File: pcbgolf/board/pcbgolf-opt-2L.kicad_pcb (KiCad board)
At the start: 2 copper layers, 48.2 x 51 mm, 245 parts, among them J1 DCBARRELSMT, J2 MICRO_SD-0472192001, J3 USB-C-FEMALE, J4 CAN, J5 USB-C-FEMALEGCT, J6 USB-C-FEMALEGCT, J7 USB-C-FEMALEGCT, J8 USB-C-FEMALEGCT, Q1 SIS427-VI, Q2 NFET-DUAL-COMMON-SOURCE-QS5K2, Q3 NFET-DUAL-COMMON-SOURCE-QS5K2, Q4 NFET-DUAL-COMMON-SOURCE-QS5K2, Q5 NFET-DUAL-COMMON-SOURCE-QS5K2, Q6 NFET-DUAL-COMMON-SOURCE-QS5K2, Q7 NFET-DUAL-COMMON-SOURCE-QS5K2, Q8 NFET-DUAL-COMMON-SOURCE-QS5K2, Q9 NFET-DUAL-COMMON-SOURCE-QS5K2, SW1 SPST-2-4PIN, U1 AP62300T, U10 NCS20071XV, U11 NCS20071XV, U12 NCS20071XV, U13 TPS25942, U14 TPS25942, U15 TPS25942, U16 TPS25942, U2 AP62300T, U3 STM32H725ZGTx, U4 USB2517, U5 MCP2542FDT-E/MNY, U6 MCP2542FDT-E/MNY, U7 MCP2542FDT-E/MNY, U8 MCP2542FDT-E/MNY, U9 NCS20071XV, Y1 25MHz, Y2 24MHz

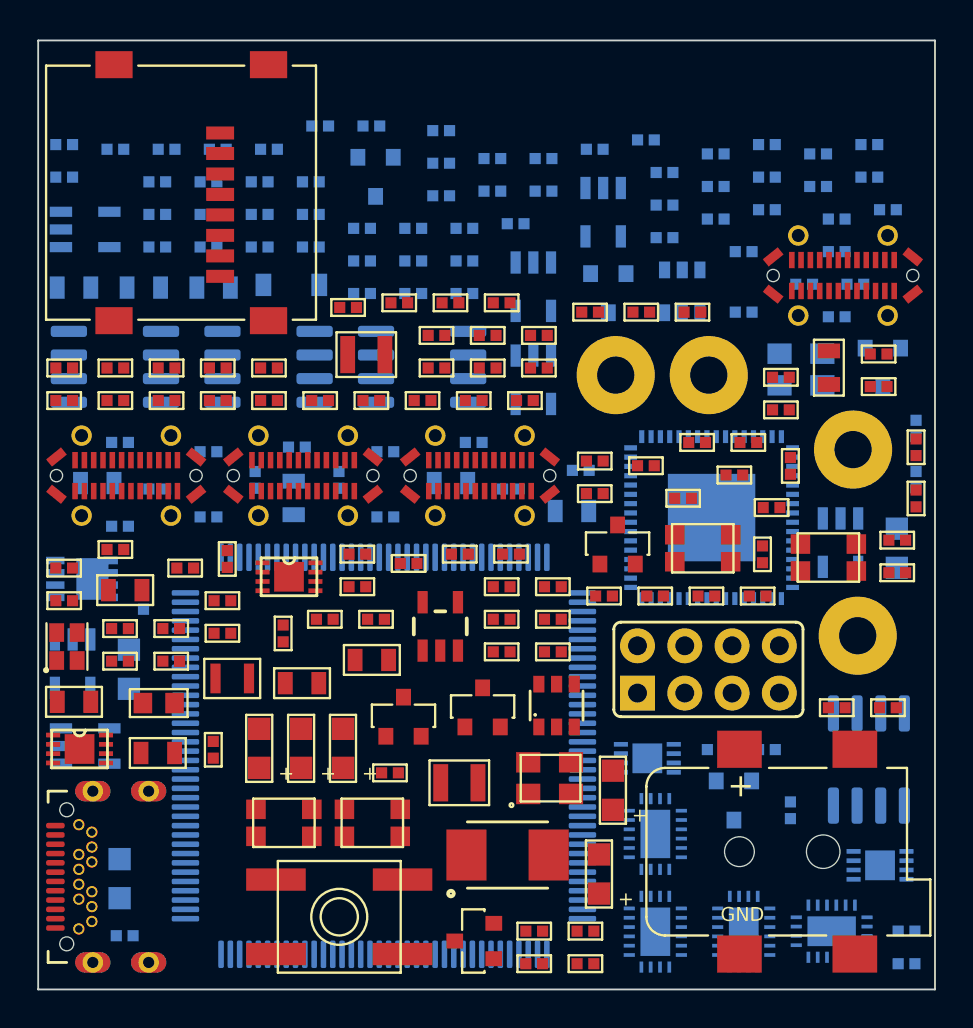
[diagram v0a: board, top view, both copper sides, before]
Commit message: Sync pcbgolf: measured part heights, 3D assembly bounding box, final board
Mirrors lblommesteyn/pcbgolf. The substantive change is that part heights are
now measured from the footprints' own STEP models rather than estimated: the
barrel jack is 11.00 mm, not the 9.00 mm assumed, so Z is 14.35 mm and every
previously reported volume was understated by about 5,300 mm^3.

Also adds bbox3d.py (the real PCBA bounding box, which is what the challenge
scores), step_assembly.py (a STEP built from that same geometry), and the
final LQFP-100 board with R11 not fitted, since the LQFP-100 package has no
PDR_ON pin for it to strap.

Co-Authored-By: Claude Opus 5 <noreply@anthropic.com>
Claude-Session: https://claude.ai/code/session_013nBHDXVrXKghy52w5PgN3h
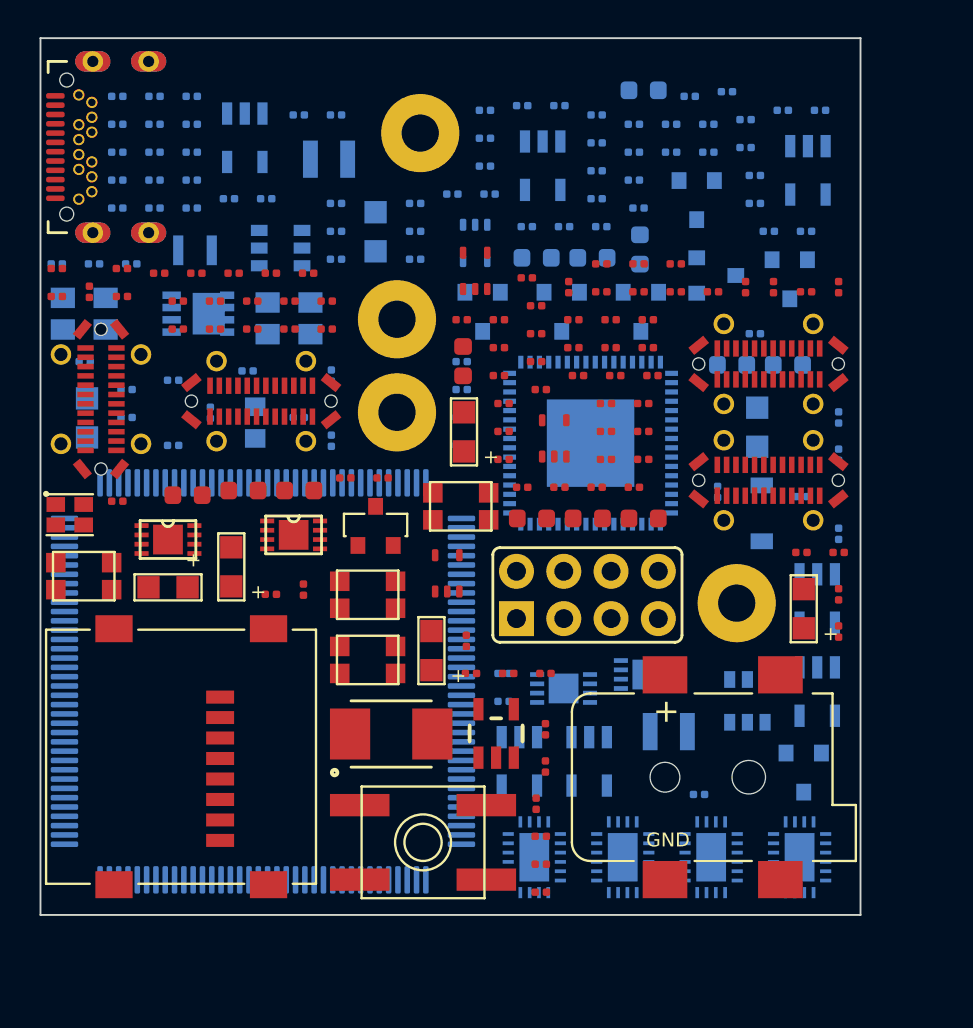
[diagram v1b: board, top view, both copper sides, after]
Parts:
- C1, C15, C19, C20, C21, C3, C50, C52, C53, C8: footprint pcbgolf:0805-C -> pcbgolf-gen:0603-C
- C10, C14, C16, C17, C18, C22, C23, C26, C28, C29, C32, C35, C36, C38, C4, C43, C44, C45, C46, C47, C48, C49, C6, C9: footprint pcbgolf:0402-C -> pcbgolf-gen:0201-C; moved to F.Cu
- C11, C24, C27, C31, C39: footprint pcbgolf:0402-C -> pcbgolf-gen:0201-C
- C12, C13: footprint pcbgolf:0805-C -> pcbgolf-gen:0603-C; moved to F.Cu
- C2, C25, C30, C33, C34, C37, C40, C41, C42, C5, C7: footprint pcbgolf:0402-C -> pcbgolf-gen:0201-C; moved to B.Cu
- C51: footprint pcbgolf:0805-C -> pcbgolf-gen:0603-C; moved to B.Cu
- L1, L2, L3, L4, LED10, LED12, LED14, LED3, LED4, LED5, Q6, U1, Y1: moved to B.Cu
- LED6, LED8, LED9, Q4: moved to F.Cu
- R1, R100, R101, R105, R106, R108, R11, R110, R111, R112, R114, R116, R117, R121, R124, R13, R14, R15, R16, R18, R19, R20, R21, R22, R24, R28, R32, R33, R36, R37, R38, R40, R44, R47, R48, R49, R50, R53, R55, R56, R57, R58, R59, R6, R60, R64, R72, R73, R74, R77, R81, R82, R83, R84, R86, R89, R9, R91, R92, R93, R95, R96, R98: footprint pcbgolf:0402-R -> pcbgolf-gen:0201-R; moved to B.Cu
- R10, R102, R103, R104, R107, R109, R113, R118, R12, R120, R122, R123, R125, R17, R23, R25, R27, R29, R3, R30, R31, R34, R35, R39, R4, R41, R42, R43, R45, R46, R5, R52, R54, R62, R63, R68, R69, R7, R71, R75, R76, R78, R79, R80, R88, R90, R94, R97, R99: footprint pcbgolf:0402-R -> pcbgolf-gen:0201-R; moved to F.Cu
- R115, R119, R2, R26, R51, R61, R65, R66, R67, R70, R8, R85, R87: footprint pcbgolf:0402-R -> pcbgolf-gen:0201-R
- U10: footprint pcbgolf:SOIC-8_3.9x4.9mm_P1.27mm -> pcbgolf-gen:SC70-5
- U11, U12, U9: footprint pcbgolf:SOIC-8_3.9x4.9mm_P1.27mm -> pcbgolf-gen:SC70-5; moved to F.Cu
- moved R30 50.0 mm to (61.3, 63.7)
- moved R28 46.9 mm to (54.1, 52.7), turned to 0 degrees
- moved R14 46.2 mm to (75.8, 53.2)
- moved C37 46.1 mm to (54.1, 57.2)
- moved C16 44.2 mm to (50.8, 61.9)
- moved Q2 44.0 mm to (91.7, 79.7), turned to 0 degrees
- moved R123 43.4 mm to (76.8, 95.4)
- moved C36 43.0 mm to (50.8, 63.4)
- moved R48 42.6 mm to (60.1, 58.2)
- moved C43 42.1 mm to (76.6, 90.7), turned to 90 degrees
- moved R77 40.9 mm to (57.1, 71.4)
- moved R62 40.5 mm to (92.8, 79.4), turned to 90 degrees
- moved J8 40.4 mm to (53.2, 68.9), turned to 90 degrees
- moved LED16 39.4 mm to (91.0, 89.0)
- moved J3 39.2 mm to (51.4, 55.4)
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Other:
- board size 48.2 x 51 mm -> 44.1 x 47.1 mm
